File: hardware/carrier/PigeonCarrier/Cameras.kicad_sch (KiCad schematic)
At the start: 0 parts

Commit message: Update carrier schematics, parts library, and JLC rules
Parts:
- added C7, C8: 1uF, PCM_JLCPCB:C_0603, symbol PCM_JLCPCB-Capacitors:0603,1uF
- added J7, J8: FH12-22S-0.5SH(55), PigeonVision:Hirose_FH12-22S-0.5SH_1x22-1MP_P0.50mm_Horizontal, symbol PigeonVision:CM5_Camera_FH12_22S_0_5SH
- added R12, R13, R14: 2.2kΩ, PCM_JLCPCB:R_0603, symbol PCM_JLCPCB-Resistors:0603,2.2kΩ
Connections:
- new net 3V3_CAM: C7.2, C8.2, J7.22 (+3V3), J8.22 (+3V3)
- new net 3V3_CM5: R12.1, R13.1, R14.1
- new net CAM0_I2C_SCL: J7.20 (SCL)
- new net CAM0_I2C_SDA: J7.21 (SDA)
- new net CAM0_RST: J7.17 (RESET)
- new net CAM1_I2C_SCL: J8.20 (SCL), R12.2
- new net CAM1_I2C_SDA: J8.21 (SDA), R13.2
- new net CAM1_RST: J8.17 (RESET), R14.2
- new net GND: C7.1, C8.1, J7.1 (GND), J7.10 (GND), J7.13 (GND), J7.16 (GND), J7.19 (GND), J7.4 (GND), J7.7 (GND), J8.1 (GND), J8.10 (GND), J8.13 (GND), J8.16 (GND), J8.19 (GND), J8.4 (GND), J8.7 (GND)
- new net MIPI0_CLK_N: J7.8 (CSI_CLK_N)
- new net MIPI0_CLK_P: J7.9 (CSI_CLK_P)
- new net MIPI0_D0_N: J7.2 (CSI_D0_N)
- new net MIPI0_D0_P: J7.3 (CSI_D0_P)
- new net MIPI0_D1_N: J7.5 (CSI_D1_N)
- new net MIPI0_D1_P: J7.6 (CSI_D1_P)
- new net MIPI0_D2_N: J7.11 (CSI_D2_N)
- new net MIPI0_D2_P: J7.12 (CSI_D2_P)
- new net MIPI0_D3_N: J7.14 (CSI_D3_N)
- new net MIPI0_D3_P: J7.15 (CSI_D3_P)
- new net MIPI1_CLK_N: J8.8 (CSI_CLK_N)
- new net MIPI1_CLK_P: J8.9 (CSI_CLK_P)
- new net MIPI1_D0_N: J8.2 (CSI_D0_N)
- new net MIPI1_D0_P: J8.3 (CSI_D0_P)
- new net MIPI1_D1_N: J8.5 (CSI_D1_N)
- new net MIPI1_D1_P: J8.6 (CSI_D1_P)
- new net MIPI1_D2_N: J8.11 (CSI_D2_N)
- new net MIPI1_D2_P: J8.12 (CSI_D2_P)
- new net MIPI1_D3_N: J8.14 (CSI_D3_N)
- new net MIPI1_D3_P: J8.15 (CSI_D3_P)
- no-connect marks 0 -> 2
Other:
- note added: "CAM0"
- note added: "CAM0 I2C: CM5 internal 1.8k pull-ups."
- note added: "CAM1"
- note added: "Camera I2C and reset pull-ups"
- note added: "Pin 18 reserved; sensor uses onboard clock."

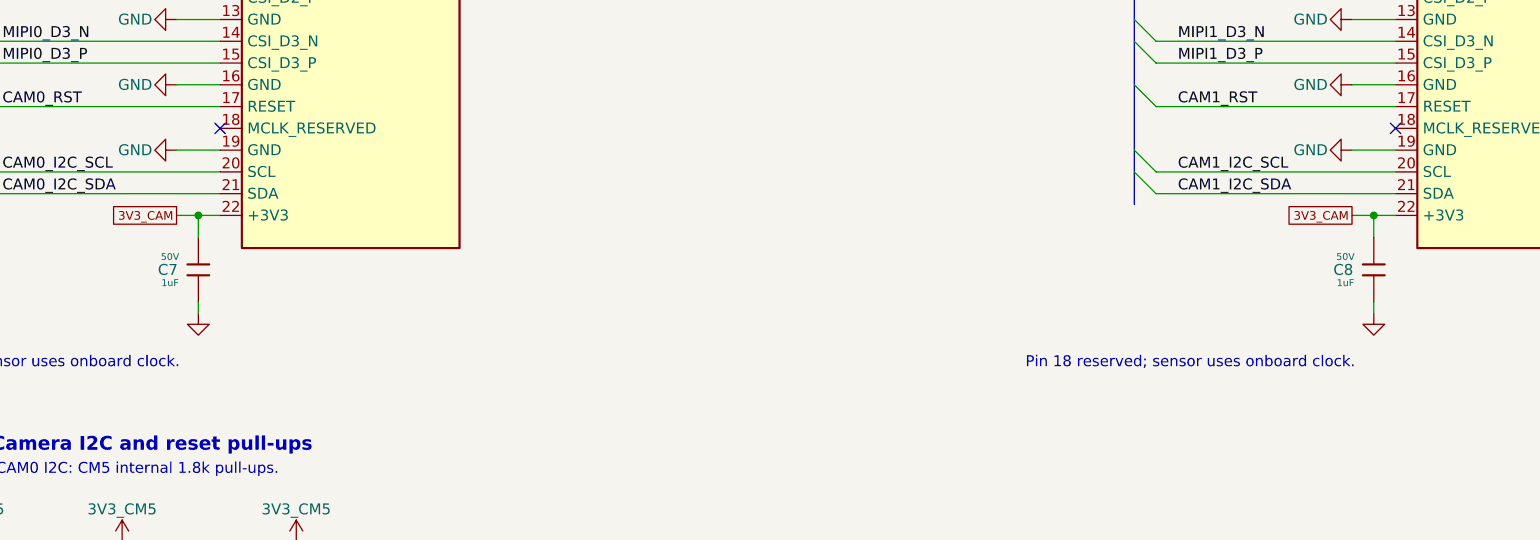
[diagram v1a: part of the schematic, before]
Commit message: Replace remaining 1 uF X5R capacitors with X7R
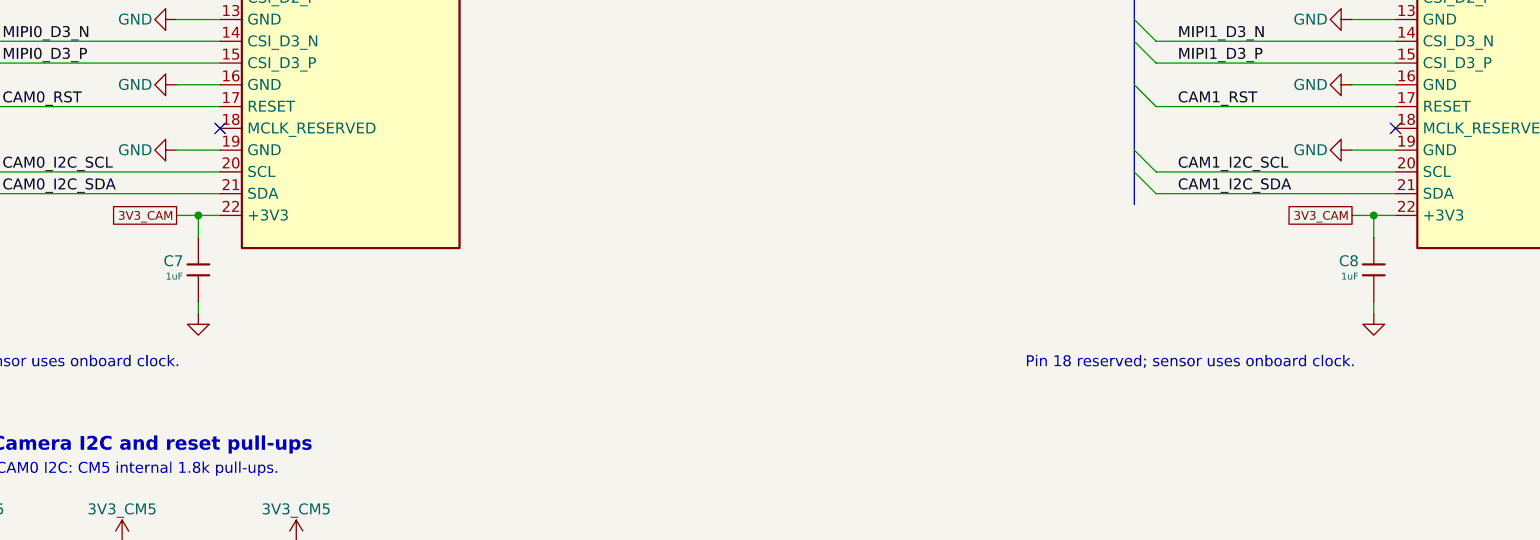
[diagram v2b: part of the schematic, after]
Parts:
- removed C7, C8: 1uF, PCM_JLCPCB:C_0603, symbol PCM_JLCPCB-Capacitors:0603,1uF
- added C7, C8: 1uF, PCM_JLCPCB:C_0805, symbol PCM_JLCPCB-Capacitors:0805,1uF
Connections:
- net 3V3_CAM: now also C7.1, C8.1
- net GND: now also C7.2, C8.2

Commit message: finished rough layout
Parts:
- C7, C8: MPN (none) -> CL21B105KBFNNNE
- R12, R13, R14: MPN (none) -> 0603WAF2201T5E
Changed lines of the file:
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@@
+			)
+		)
+		(property "MPN" "CL21B105KBFNNNE"
+			(at 73.66 102.87 0)
+			(hide yes)
+			(show_name no)
+			(do_not_autoplace no)
+			(effects
+				(font
+					(size 1.27 1.27)
+				)
 			)
 		)
@@
 			)
 		)
+		(property "MPN" "0603WAF2201T5E"
+			(at 85.09 140.97 0)
+			(hide yes)
+			(show_name no)
+			(do_not_autoplace no)
+			(effects
+				(font
+					(size 1.27 1.27)
+				)
+			)
+		)
 		(pin "1"
 		)
@@
 		)
 		(property "Temperature Coefficient" "X7R"
+			(at 210.82 102.87 0)
+			(hide yes)
+			(show_name no)
+			(do_not_autoplace no)
+			(effects
+				(font
+					(size 1.27 1.27)
+				)
+			)
+		)
+		(property "MPN" "CL21B105KBFNNNE"
 			(at 210.82 102.87 0)
 			(hide yes)
@@
 			)
 		)
+		(property "MPN" "0603WAF2201T5E"
+			(at 64.77 140.97 0)
+			(hide yes)
+			(show_name no)
+			(do_not_autoplace no)
+			(effects
+				(font
+					(size 1.27 1.27)
+				)
+			)
+		)
 		(pin "1"
 		)
@@
 			(at 46.99 140.97 0)
 			(hide yes)
+			(show_name no)
+			(do_not_autoplace no)
+			(effects
+				(font
+					(size 1.27 1.27)
+				)
+			)
+		)
+		(property "MPN" "0603WAF2201T5E"
+			(at 46.99 140.97 0)
+			(hide yes)

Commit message: Update carrier placement and vertical connector libraries
Save the latest component placements and mechanical mounting changes. Include the vertical XT60/XT30 and camera connector symbols, footprints, redistributable CAD, licenses and documentation. Keep local-only vendor models ignored.

Validation: ERC has zero findings. Native KiCad loading and netlist comparison confirm all 152 schematic components and 681 numbered pads agree. Full DRC could not complete because the KiCad CLI aborted in this environment.
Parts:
- J7, J8: value FH12-22S-0.5SH(55) -> FH12-22S-0.5SVA(54); footprint PigeonVision:Hirose_FH12-22S-0.5SH_1x22-1MP_P0.50mm_Horizontal -> PigeonVision:Hirose_FH12-22S-0.5SVA_1x22_P0.50mm_Vertical; symbol PigeonVision:CM5_Camera_FH12_22S_0_5SH -> PigeonVision:CM5_Camera_FH12_22S_0_5SVA; 3D appearance (none) -> White local presentation copy. Original Hirose STEP preserv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; DigiKey Part # HFJ122CT-ND -> (none); JLC Part # (none) -> C6250833; LCSC Part # C597981 -> C6250833; MPN FH12-22S-0.5SH(55) -> FH12-22S-0.5SVA(54); Manufacturer Hirose Electric -> Hirose
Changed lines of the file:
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@@
 	)
 	(symbol
-		(lib_id "PigeonVision:CM5_Camera_FH12_22S_0_5SH")
+		(lib_id "PigeonVision:CM5_Camera_FH12_22S_0_5SVA")
 		(at 91.44 71.12 0)
 		(unit 1)
@@
 			)
 		)
-		(property "Value" "FH12-22S-0.5SH(55)"
+		(property "Value" "FH12-22S-0.5SVA(54)"
 			(at 91.44 40.64 0)
 			(show_name no)
@@
 			)
 		)
-		(property "Footprint" "PigeonVision:Hirose_FH12-22S-0.5SH_1x22-1MP_P0.50mm_Horizontal"
+		(property "Footprint" "PigeonVision:Hirose_FH12-22S-0.5SVA_1x22_P0.50mm_Vertical"
 			(at 91.44 71.12 0)
 			(hide yes)
@@
 			)
 		)
-		(property "Datasheet" "https://www.hirose.com/en/product/p/CL0586-0532-7-55"
+		(property "Datasheet" "https://www.hirose.com/en/product/p/CL0586-0813-6-54"
 			(at 91.44 71.12 0)
 			(hide yes)
@@
 			)
 		)
-		(property "Description" "CM5IO 22-pin 0.5mm bottom-contact camera FFC: four CSI data lanes, clock, reset, I2C,3.3V. Pin18 secondary-control/MCLK reserved. 0.3+/-0.05mm FFC; MP pads mechanical."
+		(property "Description" "CM5/FRAMOS P22 camera pinout on Hirose vertical 22-pin ZIF FFC;0.5mm contact pitch,1mm PCB pitch in each staggered row;0.3+/-0.05mm ribbon;0.5A/contact. Four hold-down lands unnumbered. Pin18 remains MCLK_RESERVED. Confirm pin1-to-pin1 cable continuity and contact face; model maximum nominal5.5mm above board."
 			(at 91.44 71.12 0)
 			(hide yes)
@@
 			)
 		)
-		(property "Manufacturer" "Hirose Electric"
+		(property "Manufacturer" "Hirose"
 			(at 91.44 71.12 0)
 			(hide yes)
@@
 			)
 		)
-		(property "MPN" "FH12-22S-0.5SH(55)"
+		(property "MPN" "FH12-22S-0.5SVA(54)"
 			(at 91.44 71.12 0)
 			(hide yes)
@@
 			)
 		)
-		(property "LCSC Part #" "C597981"
+		(property "LCSC Part #" "C6250833"
 			(at 91.44 71.12 0)
 			(hide yes)
@@
 			)
 		)
-		(property "DigiKey Part #" "HFJ122CT-ND"
+		(property "DigiKey Part #" ""
 			(at 91.44 71.12 0)
 			(hide yes)
@@
 			)
 		)
-	)
+	(property "JLC Part #" "C6250833" (at 91.44 71.12 0) (hide yes) (effects (font (size 1.27 1.27))))
+	(property "3D appearance" "White local presentation copy. Original Hirose STEP preserved; all geometry and topology bytes unchanged; display color is not the physical part color specification." (at 91.44 71.12 0) (hide yes) (effects (font (size 1.27 1.27))))
+)
 	(symbol
 		(lib_id "PCM_SparkFun-PowerSymbol:GND")
@@
 	)
 	(symbol
-		(lib_id "PigeonVision:CM5_Camera_FH12_22S_0_5SH")
+		(lib_id "PigeonVision:CM5_Camera_FH12_22S_0_5SVA")
 		(at 228.6 71.12 0)
 		(unit 1)
@@
 			)
 		)
-		(property "Value" "FH12-22S-0.5SH(55)"
+		(property "Value" "FH12-22S-0.5SVA(54)"
 			(at 228.6 40.64 0)
 			(show_name no)
@@
 			)
 		)
-		(property "Footprint" "PigeonVision:Hirose_FH12-22S-0.5SH_1x22-1MP_P0.50mm_Horizontal"
+		(property "Footprint" "PigeonVision:Hirose_FH12-22S-0.5SVA_1x22_P0.50mm_Vertical"
 			(at 228.6 71.12 0)
 			(hide yes)
@@
 			)
 		)
-		(property "Datasheet" "https://www.hirose.com/en/product/p/CL0586-0532-7-55"
+		(property "Datasheet" "https://www.hirose.com/en/product/p/CL0586-0813-6-54"
 			(at 228.6 71.12 0)
 			(hide yes)
@@
 			)
 		)
-		(property "Description" "CM5IO 22-pin 0.5mm bottom-contact camera FFC: four CSI data lanes, clock, reset, I2C,3.3V. Pin18 secondary-control/MCLK reserved. 0.3+/-0.05mm FFC; MP pads mechanical."
+		(property "Description" "CM5/FRAMOS P22 camera pinout on Hirose vertical 22-pin ZIF FFC;0.5mm contact pitch,1mm PCB pitch in each staggered row;0.3+/-0.05mm ribbon;0.5A/contact. Four hold-down lands unnumbered. Pin18 remains MCLK_RESERVED. Confirm pin1-to-pin1 cable continuity and contact face; model maximum nominal5.5mm above board."
 			(at 228.6 71.12 0)
 			(hide yes)
@@
 			)
 		)
-		(property "Manufacturer" "Hirose Electric"
+		(property "Manufacturer" "Hirose"
 			(at 228.6 71.12 0)
 			(hide yes)
@@
 			)
 		)
-		(property "MPN" "FH12-22S-0.5SH(55)"
+		(property "MPN" "FH12-22S-0.5SVA(54)"
 			(at 228.6 71.12 0)
 			(hide yes)
@@
 			)
 		)
-		(property "LCSC Part #" "C597981"
+		(property "LCSC Part #" "C6250833"
 			(at 228.6 71.12 0)
 			(hide yes)
@@
 			)
 		)
-		(property "DigiKey Part #" "HFJ122CT-ND"
+		(property "DigiKey Part #" ""
 			(at 228.6 71.12 0)
 			(hide yes)
@@
 			)
 		)
-	)
+	(property "JLC Part #" "C6250833" (at 228.6 71.12 0) (hide yes) (effects (font (size 1.27 1.27))))
+	(property "3D appearance" "White local presentation copy. Original Hirose STEP preserved; all geometry and topology bytes unchanged; display color is not the physical part color specification." (at 228.6 71.12 0) (hide yes) (effects (font (size 1.27 1.27))))
+)
 	(symbol
 		(lib_id "PCM_SparkFun-PowerSymbol:GND")
